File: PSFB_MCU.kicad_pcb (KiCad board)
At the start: 4 copper layers, 293 parts, among them J2 Power_IN, Q1 WMM043N10HGD, Q2 WMM043N10HGD, Q3 WMM043N10HGD, Q4 WMM043N10HGD, U10 USBLC6-2SC6, U11 USBLC6-2SC6, U12 USBLC6-2SC6, U13 USBLC6-2SC6, U14 USBLC6-2SC6, U17 TLV3501AIDBV, U19 TLV3501AIDBV, U20 TLV3501AIDBV, U4 AMS1117-5.0, U5 AMS1117-3.3, U6 LM5176PWP, U7 USBLC6-2SC6, U8 USBLC6-2SC6, U9 USBLC6-2SC6, Y1 16M

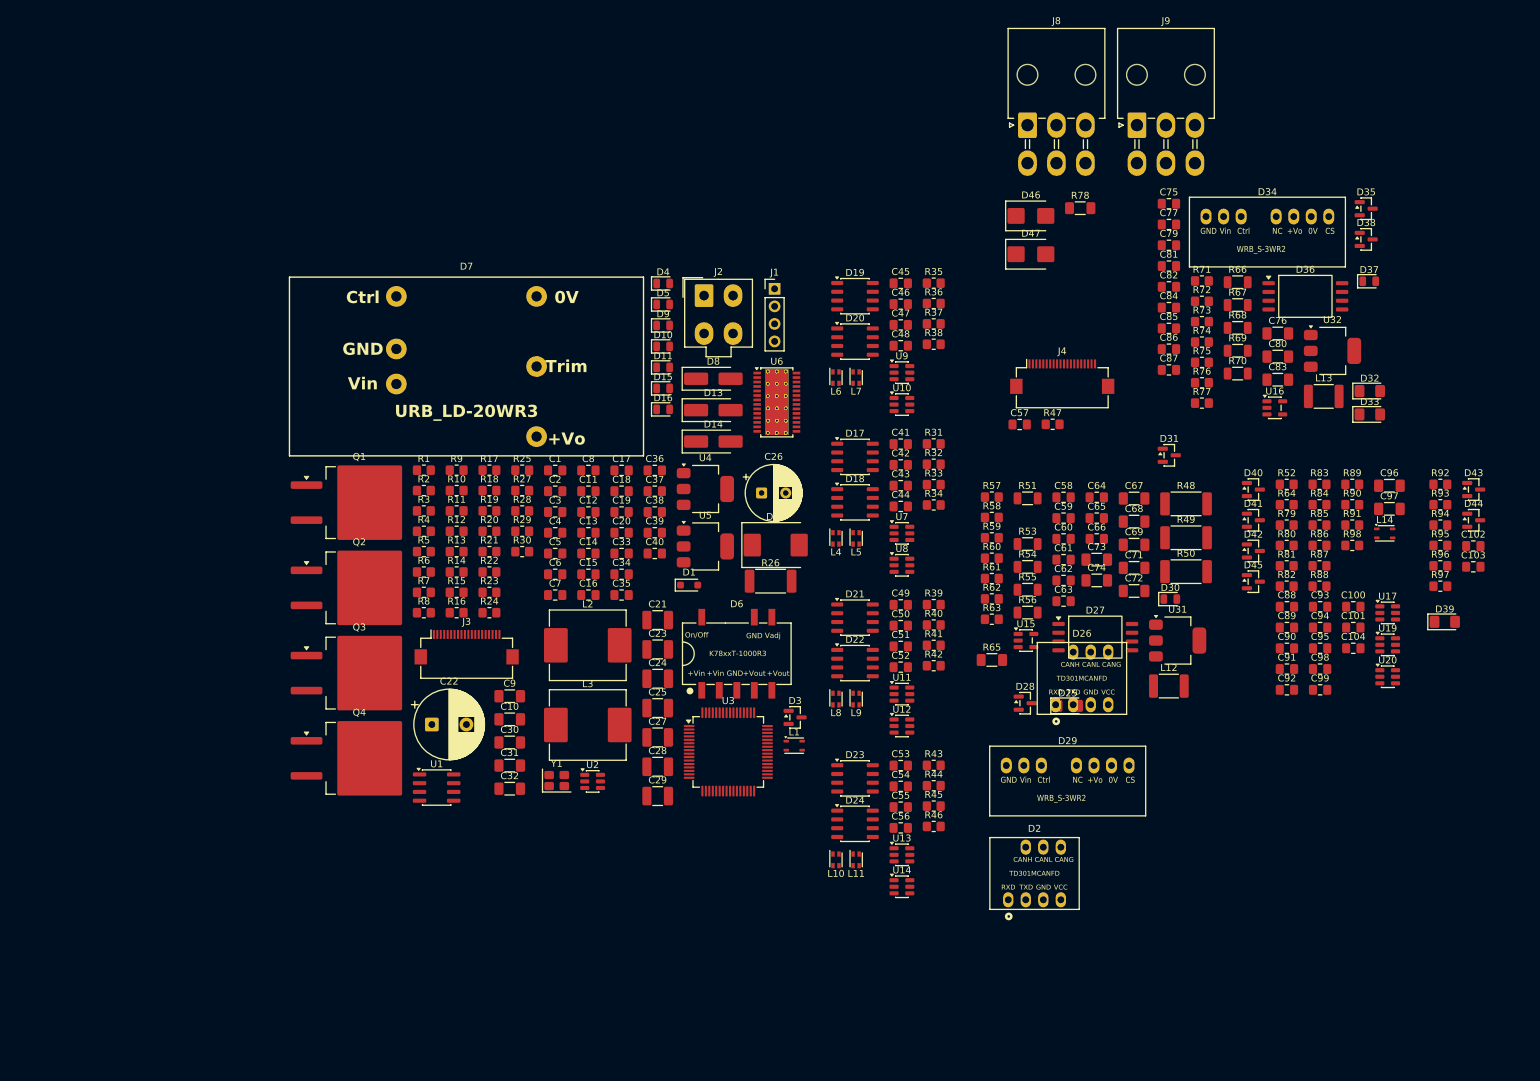
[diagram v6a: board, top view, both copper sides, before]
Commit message: VER1.0: добавил разделение питания VDD и VDDA
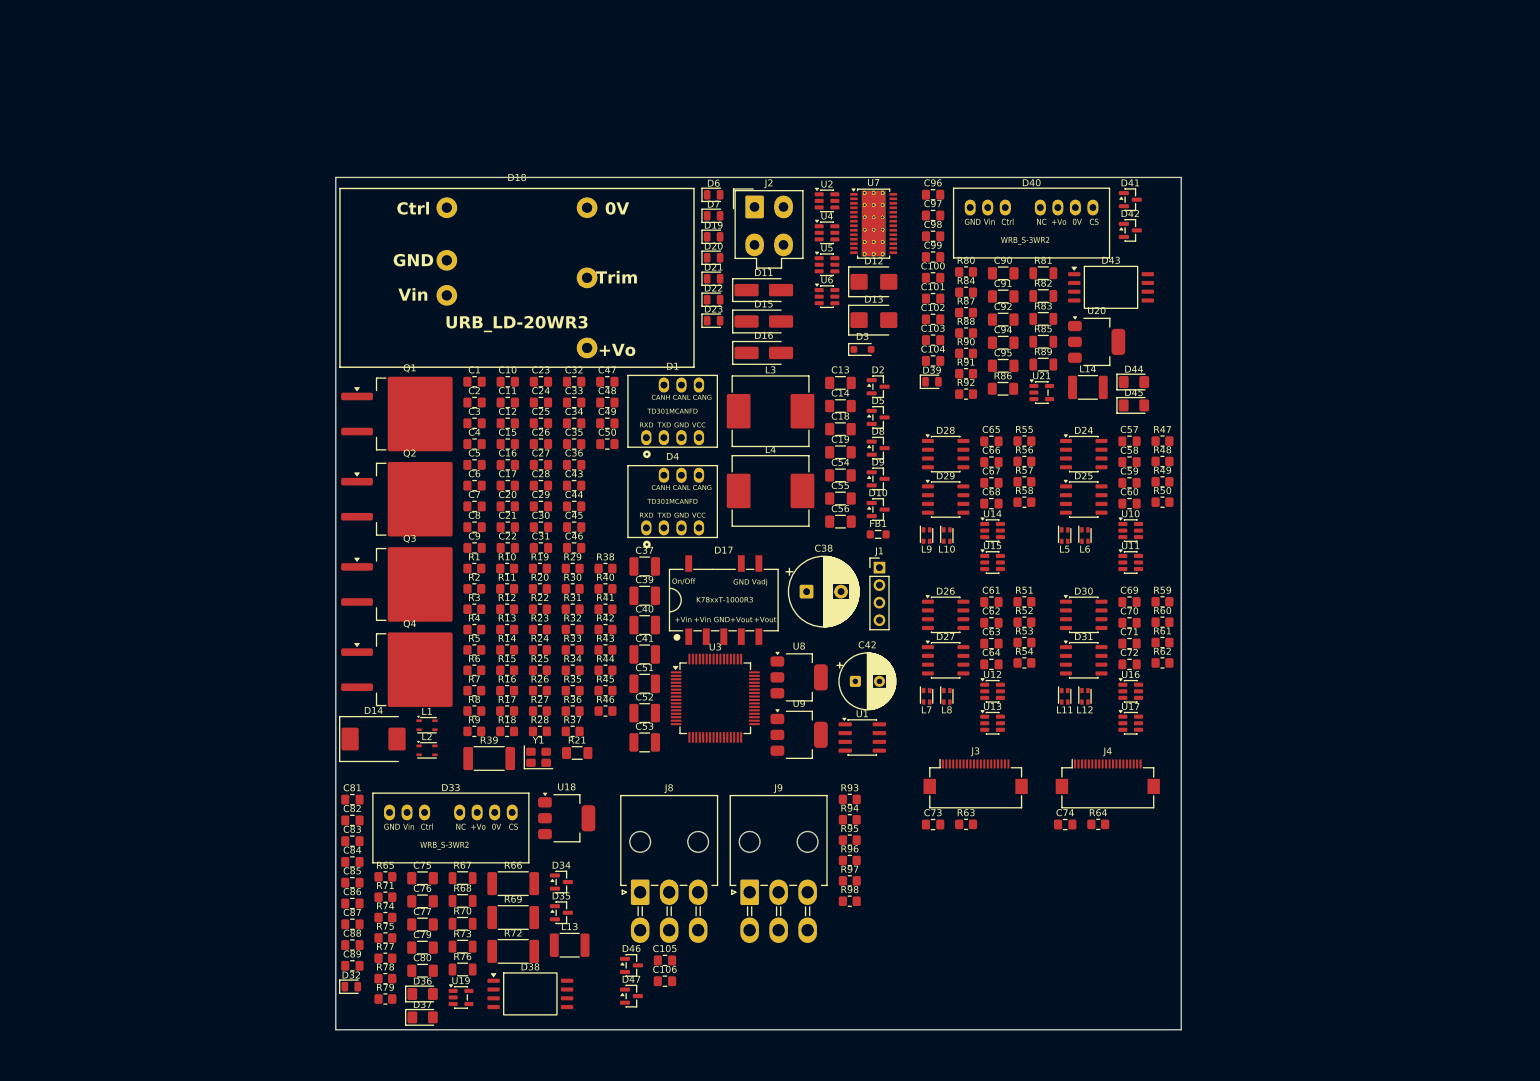
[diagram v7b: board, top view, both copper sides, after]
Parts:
- removed C93: 2.2u, Capacitor_SMD:C_0805_2012Metric_Pad1.18x1.45mm_HandSolder
- removed U31, U32: ~, Package_TO_SOT_SMD:SOT-223-3_TabPin2
- added C105: 330p, Capacitor_SMD:C_0805_2012Metric_Pad1.18x1.45mm_HandSolder, F.Cu at (130.2, 150.0)
- added C106: 330p, Capacitor_SMD:C_0805_2012Metric_Pad1.18x1.45mm_HandSolder, F.Cu at (130.2, 153.0)
- added C70: 4.7u, Capacitor_SMD:C_0805_2012Metric_Pad1.18x1.45mm_HandSolder, F.Cu at (197.5, 101.0)
- added FB1: ~, Inductor_SMD:L_0805_2012Metric_Pad1.05x1.20mm_HandSolder, F.Cu at (161.1, 88.2)
- added U18: ~, Package_TO_SOT_SMD:SOT-223-3_TabPin2, F.Cu at (116.0, 129.3)
- added U21: ~, Package_TO_SOT_SMD:SOT-23-5, F.Cu at (184.8, 67.7)
- C1: value 1u -> 100n
- C10: value 100n -> 10u; footprint Capacitor_SMD:C_1206_3216Metric_Pad1.33x1.80mm_HandSolder -> Capacitor_SMD:C_0805_2012Metric_Pad1.18x1.45mm_HandSolder
- C100: value 100n -> 56p
- C101, C86, C88: value 100n -> 2.2u
- C102: value 330p -> 0.1u
- C103: value 330p -> 2.2u
- C104: value 10n -> 0.1u
- C11: value 10n -> 1u
- C12, C59, C61: value 2.2u -> 100n
- C13, C77, C94: value 2.2u -> 10u; footprint Capacitor_SMD:C_0805_2012Metric_Pad1.18x1.45mm_HandSolder -> Capacitor_SMD:C_1206_3216Metric_Pad1.33x1.80mm_HandSolder
- C14: footprint Capacitor_SMD:C_0805_2012Metric_Pad1.18x1.45mm_HandSolder -> Capacitor_SMD:C_1206_3216Metric_Pad1.33x1.80mm_HandSolder
- C15, C20: value 100n -> 10n
- C16: value 4.7u -> 12p
- C17: value 1u -> 12p
- C18, C54, C92, C95: value 100n -> 10u; footprint Capacitor_SMD:C_0805_2012Metric_Pad1.18x1.45mm_HandSolder -> Capacitor_SMD:C_1206_3216Metric_Pad1.33x1.80mm_HandSolder
- C19: value 1u -> 100n; footprint Capacitor_SMD:C_0805_2012Metric_Pad1.18x1.45mm_HandSolder -> Capacitor_SMD:C_1206_3216Metric_Pad1.33x1.80mm_HandSolder
- C21: footprint Capacitor_SMD:C_1210_3225Metric_Pad1.33x2.70mm_HandSolder -> Capacitor_SMD:C_0805_2012Metric_Pad1.18x1.45mm_HandSolder
- C22: value 100u -> 2.2u; footprint Capacitor_THT:CP_Radial_D10.0mm_P5.00mm -> Capacitor_SMD:C_0805_2012Metric_Pad1.18x1.45mm_HandSolder
- C23: value 4.7u -> 2.2u; footprint Capacitor_SMD:C_1210_3225Metric_Pad1.33x2.70mm_HandSolder -> Capacitor_SMD:C_0805_2012Metric_Pad1.18x1.45mm_HandSolder
- C24, C28: value 10u -> 100n; footprint Capacitor_SMD:C_1210_3225Metric_Pad1.33x2.70mm_HandSolder -> Capacitor_SMD:C_0805_2012Metric_Pad1.18x1.45mm_HandSolder
- C25, C29: value 10u -> 10p; footprint Capacitor_SMD:C_1210_3225Metric_Pad1.33x2.70mm_HandSolder -> Capacitor_SMD:C_0805_2012Metric_Pad1.18x1.45mm_HandSolder
- C26: value 220u -> 100n; footprint Capacitor_THT:CP_Radial_D8.0mm_P3.50mm -> Capacitor_SMD:C_0805_2012Metric_Pad1.18x1.45mm_HandSolder
- C27: value 10u -> 2.2u; footprint Capacitor_SMD:C_1210_3225Metric_Pad1.33x2.70mm_HandSolder -> Capacitor_SMD:C_0805_2012Metric_Pad1.18x1.45mm_HandSolder
- C3, C4: value 12p -> 100n
- C30, C32, C67, C69, C71: value 10u -> 100n; footprint Capacitor_SMD:C_1206_3216Metric_Pad1.33x1.80mm_HandSolder -> Capacitor_SMD:C_0805_2012Metric_Pad1.18x1.45mm_HandSolder
- C31: value 10u -> 2.2u; footprint Capacitor_SMD:C_1206_3216Metric_Pad1.33x1.80mm_HandSolder -> Capacitor_SMD:C_0805_2012Metric_Pad1.18x1.45mm_HandSolder
- C33: value 33n -> 100n
- C34, C8: value 100n -> 1u
- C35: value 560p -> 100n
- C36: value 100n -> 10p
- C37: value 220p -> 2.2u; footprint Capacitor_SMD:C_0805_2012Metric_Pad1.18x1.45mm_HandSolder -> Capacitor_SMD:C_1210_3225Metric_Pad1.33x2.70mm_HandSolder
- C38: value 100n -> 100u; footprint Capacitor_SMD:C_0805_2012Metric_Pad1.18x1.45mm_HandSolder -> Capacitor_THT:CP_Radial_D10.0mm_P5.00mm
- C39: value 47p -> 4.7u; footprint Capacitor_SMD:C_0805_2012Metric_Pad1.18x1.45mm_HandSolder -> Capacitor_SMD:C_1210_3225Metric_Pad1.33x2.70mm_HandSolder
- C40: value 10n -> 10u; footprint Capacitor_SMD:C_0805_2012Metric_Pad1.18x1.45mm_HandSolder -> Capacitor_SMD:C_1210_3225Metric_Pad1.33x2.70mm_HandSolder
- C41, C53: value 100n -> 10u; footprint Capacitor_SMD:C_0805_2012Metric_Pad1.18x1.45mm_HandSolder -> Capacitor_SMD:C_1210_3225Metric_Pad1.33x2.70mm_HandSolder
- C42: value 4.7u -> 220u; footprint Capacitor_SMD:C_0805_2012Metric_Pad1.18x1.45mm_HandSolder -> Capacitor_THT:CP_Radial_D8.0mm_P3.50mm
- C44: value 4.7u -> 33n
- C46: value 100n -> 560p
- C47: value 4.7u -> 100n
- C48: value 4.7u -> 220p
- C50: value 100n -> 47p
- C51, C52: value 4.7u -> 10u; footprint Capacitor_SMD:C_0805_2012Metric_Pad1.18x1.45mm_HandSolder -> Capacitor_SMD:C_1210_3225Metric_Pad1.33x2.70mm_HandSolder
- C55, C56: value 4.7u -> 10u; footprint Capacitor_SMD:C_0805_2012Metric_Pad1.18x1.45mm_HandSolder -> Capacitor_SMD:C_1206_3216Metric_Pad1.33x1.80mm_HandSolder
- C57: value 10n -> 100n
- C58, C64: value 56p -> 4.7u
- C60, C62: value 0.1u -> 4.7u
- C63: value 56p -> 100n
- C66: value 1n -> 4.7u
- C68: value 1u -> 4.7u; footprint Capacitor_SMD:C_1206_3216Metric_Pad1.33x1.80mm_HandSolder -> Capacitor_SMD:C_0805_2012Metric_Pad1.18x1.45mm_HandSolder
- C7: value 100n -> 4.7u
- C72: value 10u -> 4.7u; footprint Capacitor_SMD:C_1206_3216Metric_Pad1.33x1.80mm_HandSolder -> Capacitor_SMD:C_0805_2012Metric_Pad1.18x1.45mm_HandSolder
- C73: value 10u -> 10n; footprint Capacitor_SMD:C_1206_3216Metric_Pad1.33x1.80mm_HandSolder -> Capacitor_SMD:C_0805_2012Metric_Pad1.18x1.45mm_HandSolder
- C74: value 1u -> 10n; footprint Capacitor_SMD:C_1206_3216Metric_Pad1.33x1.80mm_HandSolder -> Capacitor_SMD:C_0805_2012Metric_Pad1.18x1.45mm_HandSolder
- C75: value 56p -> 10u; footprint Capacitor_SMD:C_0805_2012Metric_Pad1.18x1.45mm_HandSolder -> Capacitor_SMD:C_1206_3216Metric_Pad1.33x1.80mm_HandSolder
- C76: value 10u -> 1u
- C79: value 0.1u -> 10u; footprint Capacitor_SMD:C_0805_2012Metric_Pad1.18x1.45mm_HandSolder -> Capacitor_SMD:C_1206_3216Metric_Pad1.33x1.80mm_HandSolder
- C81: value 2.2u -> 56p
- C82: value 0.1u -> 100n
- C83, C96: value 10u -> 56p; footprint Capacitor_SMD:C_1206_3216Metric_Pad1.33x1.80mm_HandSolder -> Capacitor_SMD:C_0805_2012Metric_Pad1.18x1.45mm_HandSolder
- C84: value 56p -> 1n
- C87: value 1n -> 0.1u
- C89: value 10p -> 0.1u
- C9, C97: footprint Capacitor_SMD:C_1206_3216Metric_Pad1.33x1.80mm_HandSolder -> Capacitor_SMD:C_0805_2012Metric_Pad1.18x1.45mm_HandSolder
- C90: value 10p -> 10u; footprint Capacitor_SMD:C_0805_2012Metric_Pad1.18x1.45mm_HandSolder -> Capacitor_SMD:C_1206_3216Metric_Pad1.33x1.80mm_HandSolder
- C91: value 100n -> 1u; footprint Capacitor_SMD:C_0805_2012Metric_Pad1.18x1.45mm_HandSolder -> Capacitor_SMD:C_1206_3216Metric_Pad1.33x1.80mm_HandSolder
- C98: value 10p -> 56p
- C99: value 2.2u -> 1n
- D1: footprint Diode_SMD:D_SOD-323_HandSoldering -> MORNSUN:TD5(3)01MCANFD
- D10, D5, D9: footprint LED_SMD:LED_0805_2012Metric -> Package_TO_SOT_SMD:SOT-23
- D11, D15, D16: footprint LED_SMD:LED_0805_2012Metric -> Diode_SMD:D_SMA_Handsoldering
- D12: value D_TVS_Small -> ~; footprint Diode_SMD:D_SMC -> Diode_SMD:D_SMB
- D13: value D_Schottky_Small -> ~; footprint Diode_SMD:D_SMA_Handsoldering -> Diode_SMD:D_SMB
- D14: value D_Schottky_Small -> ~; footprint Diode_SMD:D_SMA_Handsoldering -> Diode_SMD:D_SMC
- D17: footprint Package_SO:SO-8_3.9x4.9mm_P1.27mm -> MORNSUN:K78xxT-1000R3
- D18: footprint Package_SO:SO-8_3.9x4.9mm_P1.27mm -> MORNSUN:URB_LD-20WR3
- D19, D20, D21, D22, D23: footprint Package_SO:SO-8_3.9x4.9mm_P1.27mm -> LED_SMD:LED_0805_2012Metric
- D2: value TD301MCANFD -> ~; footprint MORNSUN:TD5(3)01MCANFD -> Package_TO_SOT_SMD:SOT-23
- D25: footprint LED_SMD:LED_1206_3216Metric_Pad1.42x1.75mm_HandSolder -> Package_SO:SO-8_3.9x4.9mm_P1.27mm
- D26: value TD301MCANFD -> ~; footprint MORNSUN:TD5(3)01MCANFD -> Package_SO:SO-8_3.9x4.9mm_P1.27mm
- D27: footprint Package_SO:SOIC-8_7.5x5.85mm_P1.27mm -> Package_SO:SO-8_3.9x4.9mm_P1.27mm
- D28, D31: footprint Package_TO_SOT_SMD:SOT-23 -> Package_SO:SO-8_3.9x4.9mm_P1.27mm
- D29: footprint MORNSUN:WRB_S-3WR2 -> Package_SO:SO-8_3.9x4.9mm_P1.27mm
- D3: footprint Package_TO_SOT_SMD:SOT-23 -> Diode_SMD:D_SOD-323_HandSoldering
- D30: footprint LED_SMD:LED_0805_2012Metric -> Package_SO:SO-8_3.9x4.9mm_P1.27mm
- D32, D39: footprint LED_SMD:LED_1206_3216Metric_Pad1.42x1.75mm_HandSolder -> LED_SMD:LED_0805_2012Metric
- D33: footprint LED_SMD:LED_1206_3216Metric_Pad1.42x1.75mm_HandSolder -> MORNSUN:WRB_S-3WR2
- D34: footprint MORNSUN:WRB_S-3WR2 -> Package_TO_SOT_SMD:SOT-23
- D36: footprint Package_SO:SOIC-8_7.5x5.85mm_P1.27mm -> LED_SMD:LED_1206_3216Metric_Pad1.42x1.75mm_HandSolder
- D37: footprint LED_SMD:LED_0805_2012Metric -> LED_SMD:LED_1206_3216Metric_Pad1.42x1.75mm_HandSolder
- D38, D43: footprint Package_TO_SOT_SMD:SOT-23 -> Package_SO:SOIC-8_7.5x5.85mm_P1.27mm
- D4: footprint LED_SMD:LED_0805_2012Metric -> MORNSUN:TD5(3)01MCANFD
- D40: footprint Package_TO_SOT_SMD:SOT-23 -> MORNSUN:WRB_S-3WR2
- D44, D45: footprint Package_TO_SOT_SMD:SOT-23 -> LED_SMD:LED_1206_3216Metric_Pad1.42x1.75mm_HandSolder
- D46: value D_TVS_Small -> ~; footprint Diode_SMD:D_SMB -> Package_TO_SOT_SMD:SOT-23
- D47: value D_Small -> ~; footprint Diode_SMD:D_SMB -> Package_TO_SOT_SMD:SOT-23
- D6: value K7809T -> ~; footprint MORNSUN:K78xxT-1000R3 -> LED_SMD:LED_0805_2012Metric
- D7: value URB2415LD-20WR3 -> ~; footprint MORNSUN:URB_LD-20WR3 -> LED_SMD:LED_0805_2012Metric
- D8: value D_Schottky_Small -> ~; footprint Diode_SMD:D_SMA_Handsoldering -> Package_TO_SOT_SMD:SOT-23
- J2: value Power_IN -> ~
- L10, L11, L5, L6, L7, L8, L9: value DLW21SN900SQ2L -> ~
- L12: value 4.7u -> ~; footprint Inductor_SMD:L_1812_4532Metric_Pad1.30x3.40mm_HandSolder -> Inductor_SMD:L_CommonModeChoke_Coilcraft_0805USB
- L14: value ~ -> 4.7u; footprint Inductor_SMD:L_CommonModeChoke_TDK_ACM2520-2P -> Inductor_SMD:L_1812_4532Metric_Pad1.30x3.40mm_HandSolder
- L2: value 10u -> ~; footprint Inductor_SMD:L_Panasonic_PCC-M1040ML -> Inductor_SMD:L_CommonModeChoke_TDK_ACM2520-2P
- L4: value DLW21SN900SQ2L -> 10u; footprint Inductor_SMD:L_CommonModeChoke_Coilcraft_0805USB -> Inductor_SMD:L_Panasonic_PCC-M1040ML
- Q1, Q2, Q3, Q4: value WMM043N10HGD -> ~
- R1, R2: value 10k -> 59
- R10: value 10 -> 1k
- R11: value 1k -> 100
- R13, R29: value 3k -> 1k
- R15: value 249k -> 100
- R16: value 59k -> 0
- R17: value 10k -> 1k
- R18: value 240k -> 0
- R19: value 93.1k -> 1k
- R20: value 51k -> 100
- R21: value 143k -> 10; footprint Resistor_SMD:R_0805_2012Metric_Pad1.20x1.40mm_HandSolder -> Resistor_SMD:R_1206_3216Metric_Pad1.30x1.75mm_HandSolder
- R22: value 10k -> 0
- R23: value 10k -> 2k
- R24: value 100 -> 10
- R25, R41, R44, R79, R88: value 0 -> 1k
- R26: value 10m -> 249k; footprint Resistor_SMD:R_2512_6332Metric_Pad1.40x3.35mm_HandSolder -> Resistor_SMD:R_0805_2012Metric_Pad1.20x1.40mm_HandSolder
- R27: value 100 -> 59k
- R28, R47: value 470 -> 0
- R3, R4: value 20 -> 10k
- R30: value 3k -> 10k
- R31: value 0 -> 240k
- R32: value 0 -> 93.1k
- R33: value 0 -> 51k
- R34: value 0 -> 143k
- R35, R36: value 0 -> 10k
- R37, R40: value 0 -> 100
- R39: value 0 -> 10m; footprint Resistor_SMD:R_0805_2012Metric_Pad1.20x1.40mm_HandSolder -> Resistor_SMD:R_2512_6332Metric_Pad1.40x3.35mm_HandSolder
- R43, R45, R46: value 0 -> 3k
- R48, R49, R50: value 150k -> 0; footprint Resistor_SMD:R_2512_6332Metric_Pad1.40x3.35mm_HandSolder -> Resistor_SMD:R_0805_2012Metric_Pad1.20x1.40mm_HandSolder
- R5, R6: value 59 -> 20
- R51, R53, R54, R55: value 2M -> 0; footprint Resistor_SMD:R_1206_3216Metric -> Resistor_SMD:R_0805_2012Metric_Pad1.20x1.40mm_HandSolder
- R52, R58, R59, R60, R61: value 1k -> 0
- R56: value 11.3k -> 0; footprint Resistor_SMD:R_1206_3216Metric -> Resistor_SMD:R_0805_2012Metric_Pad1.20x1.40mm_HandSolder
- R57: value 120 -> 0
- R62: value 510 -> 0
- R63: value 750 -> 470
- R64: value 1k -> 470
- R65: value 10k -> 750; footprint Resistor_SMD:R_1206_3216Metric_Pad1.30x1.75mm_HandSolder -> Resistor_SMD:R_0805_2012Metric_Pad1.20x1.40mm_HandSolder
- R66, R69: value 110k -> 150k; footprint Resistor_SMD:R_1206_3216Metric -> Resistor_SMD:R_2512_6332Metric_Pad1.40x3.35mm_HandSolder
- R67, R68: value 110k -> 2M
- R7, R8: value 1k -> 59
- R70: value 11.3k -> 2M
- R71: value 120 -> 1k
- R72: value 1k -> 150k; footprint Resistor_SMD:R_0805_2012Metric_Pad1.20x1.40mm_HandSolder -> Resistor_SMD:R_2512_6332Metric_Pad1.40x3.35mm_HandSolder
- R73: value 1k -> 2M; footprint Resistor_SMD:R_0805_2012Metric_Pad1.20x1.40mm_HandSolder -> Resistor_SMD:R_1206_3216Metric
- R74: value 750 -> 120
- R76: value 1k -> 11.3k; footprint Resistor_SMD:R_0805_2012Metric_Pad1.20x1.40mm_HandSolder -> Resistor_SMD:R_1206_3216Metric
- R78: value 10 -> 1k; footprint Resistor_SMD:R_1206_3216Metric_Pad1.30x1.75mm_HandSolder -> Resistor_SMD:R_0805_2012Metric_Pad1.20x1.40mm_HandSolder
- R80: value 100 -> 750
- R81: value 100 -> 110k; footprint Resistor_SMD:R_0805_2012Metric_Pad1.20x1.40mm_HandSolder -> Resistor_SMD:R_1206_3216Metric
- R82, R83: value 0 -> 110k; footprint Resistor_SMD:R_0805_2012Metric_Pad1.20x1.40mm_HandSolder -> Resistor_SMD:R_1206_3216Metric
- R85: value 1k -> 110k; footprint Resistor_SMD:R_0805_2012Metric_Pad1.20x1.40mm_HandSolder -> Resistor_SMD:R_1206_3216Metric
- R86: value 59 -> 10k; footprint Resistor_SMD:R_0805_2012Metric_Pad1.20x1.40mm_HandSolder -> Resistor_SMD:R_1206_3216Metric_Pad1.30x1.75mm_HandSolder
- R87: value 100 -> 120
- R89: value 0 -> 11.3k; footprint Resistor_SMD:R_0805_2012Metric_Pad1.20x1.40mm_HandSolder -> Resistor_SMD:R_1206_3216Metric
- R9, R92: value 2k -> 1k
- R90: value 1k -> 510
- R93: value 3k -> 2k
- R95: value 120 -> 3k
- R97: value 3k -> 120
- R98: value 59 -> 3k
- U10, U11, U12, U13, U14: value USBLC6-2SC6 -> ~
- U15, U16: footprint Package_TO_SOT_SMD:SOT-23-5 -> Package_TO_SOT_SMD:SOT-23-6
- U17: value TLV3501AIDBV -> ~
- U19: value TLV3501AIDBV -> ~; footprint Package_TO_SOT_SMD:SOT-23-6 -> Package_TO_SOT_SMD:SOT-23-5
- U20: value TLV3501AIDBV -> ~; footprint Package_TO_SOT_SMD:SOT-23-6 -> Package_TO_SOT_SMD:SOT-223-3_TabPin2
- U4: value AMS1117-5.0 -> ~; footprint Package_TO_SOT_SMD:SOT-223-3_TabPin2 -> Package_TO_SOT_SMD:SOT-23-6
- U5: value AMS1117-3.3 -> ~; footprint Package_TO_SOT_SMD:SOT-223-3_TabPin2 -> Package_TO_SOT_SMD:SOT-23-6
- U6: value LM5176PWP -> ~; footprint Package_SO:HTSSOP-28-1EP_4.4x9.7mm_P0.65mm_EP3.4x9.5mm_ThermalVias -> Package_TO_SOT_SMD:SOT-23-6
- U7: value USBLC6-2SC6 -> ~; footprint Package_TO_SOT_SMD:SOT-23-6 -> Package_SO:HTSSOP-28-1EP_4.4x9.7mm_P0.65mm_EP3.4x9.5mm_ThermalVias
- U8, U9: value USBLC6-2SC6 -> ~; footprint Package_TO_SOT_SMD:SOT-23-6 -> Package_TO_SOT_SMD:SOT-223-3_TabPin2
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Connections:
- C100 pad 1: +3.3V -> Net-(U21--)
- C100 pad 2: GND -> Net-(C100-Pad2)
- C101 pad 1: Net-(U20--) -> GND_OUT
- C101 pad 2: GND -> +3.3VP
- C102 pad 1: /Current_measure_1 -> +3.3VP
- C102 pad 2: GND -> GND_OUT
- C103 pad 1: /Current_measure_2 -> GND
- C103 pad 2: GND -> +3.3VA
- C104 pad 1: Net-(C104-Pad1) -> +3.3VA
- C104 pad 2: GND_CAN2 -> GND
- C11 pad 1: Net-(C11-Pad1) -> +3.3V
- C11 pad 2: GND_CAN1 -> GND
- C12 pad 1: Net-(U3-VCAP_1) -> GND
- C12 pad 2: GND -> NRST
- C13 pad 1: Net-(U3-VCAP_2) -> +3.3V
- C15 pad 1: +3.3V -> Net-(C15-Pad1)
- C15 pad 2: GND -> GND_CAN1
- C16 pad 1: +3.3V -> GND
- C16 pad 2: GND -> Net-(U3-PH0)
- C17 pad 1: +3.3V -> Net-(U3-PH1)
- C18 pad 1: Net-(U6-VIN) -> +3.3V
- C18 pad 2: GND_IN -> GND
- C19 pad 1: VCC -> +3.3V
- C19 pad 2: GND_IN -> GND
- C2 pad 1: GND -> +3.3V
- C2 pad 2: NRST -> GND
- C20 pad 1: +24V -> Net-(C20-Pad1)
- C20 pad 2: GND_IN -> GND_CAN2
- C21 pad 1: GND_IN -> Net-(U3-VCAP_1)
- C21 pad 2: Net-(D12-A2) -> GND
- C22 pad 1: Net-(D12-A2) -> Net-(U3-VCAP_2)
- C22 pad 2: GND_IN -> GND
- C23 pad 1: GND_IN -> +3.3VA
- C23 pad 2: Net-(D12-A2) -> GND
- C24 pad 1: GND_IN -> +3.3VA
- C24 pad 2: +24V -> GND
- C25 pad 1: GND_IN -> /OverVoltage
- C25 pad 2: +24V -> GND
- C26 pad 1: +24V -> Net-(U4--)
- C26 pad 2: GND_IN -> GND
- C27 pad 1: GND_IN -> +3.3VA
- C27 pad 2: +24V -> GND
- C28 pad 1: GND -> +3.3VA
- C28 pad 2: +15V -> GND
- C29 pad 1: GND -> /BkIN_1
- C29 pad 2: +9V -> GND
- C3 pad 1: GND -> +3.3V
- C3 pad 2: Net-(U3-PH0) -> GND
- C30 pad 1: GND -> Net-(U5--)
- C30 pad 2: +5V -> GND
- C31 pad 1: GND -> +3.3VA
- C31 pad 2: +5V -> GND
- C32 pad 1: GND -> +3.3VA
- C32 pad 2: +3.3V -> GND
- C33 pad 1: Net-(U6-COMP) -> Net-(U7-VIN)
- C33 pad 2: Net-(C33-Pad2) -> GND_IN
- C34 pad 1: Net-(U6-SS) -> VCC
- C35 pad 1: Net-(U6-COMP) -> +24V
- C36 pad 1: /SW1 -> /BkIN_8
- C36 pad 2: Net-(D13-K) -> GND
- C37 pad 1: Net-(U6-SLOPE) -> GND_IN
- C37 pad 2: GND_IN -> Net-(D14-A2)
- C38 pad 1: /SW2 -> Net-(D14-A2)
- C38 pad 2: Net-(D14-K) -> GND_IN
- C39 pad 1: Net-(U6-CSG) -> GND_IN
- C39 pad 2: Net-(U6-CS) -> Net-(D14-A2)
- C4 pad 1: Net-(U3-PH1) -> +3.3V
- C40 pad 1: /ERROR_Channel_1 -> GND_IN
- C40 pad 2: GND -> +24V
- C41 pad 1: +3.3V -> GND_IN
- C41 pad 2: GND -> +24V
- C42 pad 1: +3.3V -> +24V
- C42 pad 2: GND -> GND_IN
- C43 pad 1: +3.3V -> Net-(U6--)
- C44 pad 1: +3.3V -> Net-(U7-COMP)
- C44 pad 2: GND -> Net-(C44-Pad2)
- C45 pad 1: +3.3V -> Net-(U7-SS)
- C45 pad 2: GND -> GND_IN
- C46 pad 1: +3.3V -> Net-(U7-COMP)
- C46 pad 2: GND -> GND_IN
- C47 pad 1: +3.3V -> /SW1
- C47 pad 2: GND -> Net-(D15-K)
- C48 pad 1: +3.3V -> Net-(U7-SLOPE)
- C48 pad 2: GND -> GND_IN
- C49 pad 1: +3.3V -> /SW2
- C49 pad 2: GND -> Net-(D16-K)
- C50 pad 1: +3.3V -> Net-(U7-CSG)
- C50 pad 2: GND -> Net-(U7-CS)
- C51 pad 1: +3.3V -> GND_IN
- C51 pad 2: GND -> +24V
- C52 pad 1: +3.3V -> GND
- C52 pad 2: GND -> +15V
- C53 pad 1: +3.3V -> GND
- C53 pad 2: GND -> +9V
- C54 pad 1: +3.3V -> GND
- C54 pad 2: GND -> +5V
- C55 pad 1: +3.3V -> GND
- C55 pad 2: GND -> +5V
- C56 pad 1: +3.3V -> GND
- C56 pad 2: GND -> +3.3V
- C57 pad 1: /ERROR_Channel_2 -> +3.3V
- C58 pad 1: Net-(D27-VIN) -> +3.3V
- C58 pad 2: GNDPWR -> GND
- C59 pad 1: GNDPWR -> +3.3V
- C59 pad 2: +3.3VP -> GND
- C60 pad 1: +3.3VP -> +3.3V
- C60 pad 2: GNDPWR -> GND
- C61 pad 1: GND -> +3.3V
- C61 pad 2: +3.3V -> GND
- C63 pad 1: GND -> +3.3V
- C63 pad 2: Net-(U15-+) -> GND
- C64 pad 1: Net-(U15--) -> +3.3V
- C64 pad 2: Net-(C64-Pad2) -> GND
- C66 pad 1: /HVDC_MCU -> +3.3V
- C67 pad 1: +24V -> +3.3V
- C67 pad 2: GND_IN -> GND
- C68 pad 1: Net-(D29-Vin) -> +3.3V
- C68 pad 2: GND_IN -> GND
- C69 pad 1: GNDPWR -> +3.3V
- C69 pad 2: Net-(D29-CS) -> GND
- C71 pad 1: GNDPWR -> +3.3V
- C71 pad 2: Net-(D29-+Vo) -> GND
- C72 pad 1: GNDPWR -> +3.3V
- C72 pad 2: +3.3VP -> GND
- C73 pad 1: +24V -> /ERROR_Channel_1
- C73 pad 2: GND_IN -> GND
- C74 pad 1: Net-(D34-Vin) -> /ERROR_Channel_2
- C74 pad 2: GND_IN -> GND
- C75 pad 1: Net-(D35-common) -> +24V
- C75 pad 2: GND_OUT -> GND_IN
- C76 pad 1: GND_OUT -> Net-(D33-Vin)
- C76 pad 2: Net-(D34-CS) -> GND_IN
- C77 pad 1: GND_OUT -> GNDPWR
- C77 pad 2: +3.3VP -> Net-(D33-CS)
- C79 pad 1: +3.3VP -> GNDPWR
- C79 pad 2: GND_OUT -> Net-(D33-+Vo)
- C80 pad 1: GND_OUT -> GNDPWR
- C80 pad 2: Net-(D34-+Vo) -> +3.3VP
- C81 pad 2: +3.3V -> Net-(U19-+)
- C82 pad 1: +3.3V -> +3.3VA
- C83 pad 1: GND_OUT -> Net-(D34-common)
- C83 pad 2: +3.3VP -> GNDPWR
- C84 pad 1: GND -> /HVDC_MCU
- C84 pad 2: Net-(U16-+) -> GND
- C85 pad 1: Net-(U16--) -> Net-(U19--)
- C86 pad 1: +3.3V -> GNDPWR
- C86 pad 2: GND -> +3.3VP
- C87 pad 1: /LVDC_MCU -> +3.3VP
- C87 pad 2: GND -> GNDPWR
- C88 pad 1: Net-(U17--) -> GND
- C88 pad 2: GND -> +3.3VA
- C89 pad 1: /OverVoltage -> +3.3VA
- C9 pad 1: +3.3V -> +3.3VA
- C90 pad 1: /BkIN_1 -> +24V
- C90 pad 2: GND -> GND_IN
- C91 pad 1: Net-(U19--) -> Net-(D40-Vin)
- C91 pad 2: GND -> GND_IN
- C92 pad 1: +3.3V -> GND_OUT
- C92 pad 2: GND -> Net-(D40-CS)
- C94 pad 1: +3.3V -> GND_OUT
- C94 pad 2: GND -> Net-(D40-+Vo)
- C95 pad 1: +3.3V -> GND_OUT
- C95 pad 2: GND -> +3.3VP
- C96 pad 1: +3.3V -> GND
- C96 pad 2: GND -> Net-(U21-+)
- C97 pad 1: +3.3V -> +3.3VA
- C98 pad 1: /BkIN_8 -> Net-(D41-common)
- C98 pad 2: GND -> GND_OUT
- C99 pad 1: +3.3V -> /LVDC_MCU
- D1 pad 1: +3.3V -> /CAN1_RXD_MCU
- D1 pad 2: Net-(D1-A) -> /CAN1_TXD_MCU
- D10 pad 1: Net-(D10-K) -> GND
- D10 pad 2: +15V -> +3.3VA
- D11 pad 2: +3.3V -> VIN_filtered
- D12 pad 1: GND_IN -> Net-(D12-K)
- D12 pad 2: Net-(D12-A2) -> VIN
- D13 pad 1: Net-(D13-K) -> GND_IN
- D13 pad 2: VCC -> VIN_filtered
- D14 pad 1: Net-(D14-K) -> GND_IN
- D14 pad 2: VCC -> Net-(D14-A2)
- D15 pad 2: VIN -> VCC
- D16 pad 2: +24V -> VCC
- D17 pad 1: unconnected-(D17-RO-Pad1) -> +15V
- D17 pad 2: GND -> +15V
- D17 pad 3: +3.3V -> GND
- D17 pad 4: /TMR1_CH1N -> +9V
- D17 pad 5: GND -> +9V
- D17 pad 6: Net-(D17-A) -> unconnected-(D17-Vadj-Pad6)
- D17 pad 7: Net-(D17-B) -> GND
- D18 pad 2: GND -> GND_IN
- D18 pad 3: +3.3V -> +24V
- D18 pad 4: /TMR1_CH1 -> +15V
- D18 pad 5: GND -> Net-(D18-Trim)
- D18 pad 6: Net-(D18-A) -> GND1
- D19 pad 1: unconnected-(D19-RO-Pad1) -> Net-(D19-K)
- D19 pad 2: GND -> +5V
- D2 pad 1: /CAN1_RXD_MCU -> /CANH_1
- D2 pad 2: /CAN1_TXD_MCU -> /CANL_1
- D2 pad 3: GND -> GND_CAN1
- D20 pad 1: unconnected-(D20-RO-Pad1) -> Net-(D20-K)
- D20 pad 2: GND -> +15V
- D21 pad 1: unconnected-(D21-RO-Pad1) -> Net-(D21-K)
- D21 pad 2: GND -> +3.3V
- D22 pad 1: unconnected-(D22-RO-Pad1) -> Net-(D22-K)
- D22 pad 2: GND -> VIN
- D23 pad 1: unconnected-(D23-RO-Pad1) -> Net-(D23-K)
- D23 pad 2: GND -> +24V
- D24 pad 4: /TMR8_CH2 -> /TMR1_CH1N
- D25 pad 1: GNDPWR -> unconnected-(D25-RO-Pad1)
- D25 pad 2: Net-(D25-A) -> GND
- D26 pad 1: /CAN2_RXD_MCU -> unconnected-(D26-RO-Pad1)
- D26 pad 2: /CAN2_TXD_MCU -> GND
- D26 pad 3: GND -> +3.3V
- D26 pad 4: +3.3V -> /TMR1_CH2N
- D26 pad 5: GND_CAN2 -> GND
- D26 pad 6: Net-(D26-CANL) -> Net-(D26-A)
- D26 pad 7: Net-(D26-CANH) -> Net-(D26-B)
- D27 pad 1: +3.3VP -> unconnected-(D27-RO-Pad1)
- D27 pad 2: Net-(D27-VIN) -> GND
- D27 pad 3: GNDPWR -> +3.3V
- D27 pad 4: GNDPWR -> /TMR1_CH2
- D27 pad 6: Net-(D27-OUTN) -> Net-(D27-A)
- D27 pad 7: Net-(D27-OUTP) -> Net-(D27-B)
- D28 pad 1: GND -> unconnected-(D28-RO-Pad1)
- D28 pad 2: +3.3V -> GND
- D28 pad 3: /HVDC_MCU -> +3.3V
- D29 pad 1: GND_IN -> unconnected-(D29-RO-Pad1)
- D29 pad 2: Net-(D29-Vin) -> GND
- D29 pad 3: unconnected-(D29-Ctrl-Pad3) -> +3.3V
- D29 pad 5: unconnected-(D29-NC-Pad5) -> GND
- D29 pad 6: Net-(D29-+Vo) -> Net-(D29-A)
- D29 pad 7: GNDPWR -> Net-(D29-B)
- D29 pad 8: Net-(D29-CS) -> +3.3V
- D3 pad 1: /CANH_1 -> +3.3V
- D3 pad 2: /CANL_1 -> Net-(D3-A)
- D30 pad 1: Net-(D30-K) -> unconnected-(D30-RO-Pad1)
- D30 pad 2: +3.3VP -> GND
- D31 pad 1: GNDPWR -> unconnected-(D31-RO-Pad1)
- D31 pad 2: +3.3VP -> GND
- D31 pad 3: Net-(D27-VIN) -> +3.3V
- D32 pad 1: GND_OUT -> Net-(D32-K)
- D32 pad 2: Net-(D32-A) -> +3.3VP
- D33 pad 1: Net-(D32-A) -> GND_IN
- D33 pad 2: GND_OUT -> Net-(D33-Vin)
- D34 pad 1: GND_IN -> GNDPWR
- D34 pad 2: Net-(D34-Vin) -> +3.3VP
- D34 pad 3: unconnected-(D34-Ctrl-Pad3) -> Net-(D34-common)
- D35 pad 1: GND_OUT -> GND
- D35 pad 2: +3.3VP -> +3.3VA
- D35 pad 3: Net-(D35-common) -> /HVDC_MCU
- D36 pad 1: +3.3VP -> Net-(D36-K)
- D36 pad 2: Net-(D35-common) -> GNDPWR
- D37 pad 1: Net-(D37-K) -> GNDPWR
- D37 pad 2: +3.3VP -> Net-(D36-K)
- D38 pad 1: GND -> +3.3VP
- D38 pad 2: +3.3V -> Net-(D34-common)
- D38 pad 3: /LVDC_MCU -> GNDPWR
- D39 pad 1: Net-(D25-A) -> Net-(D39-K)
- D39 pad 2: GNDPWR -> +3.3VP
- D4 pad 1: Net-(D4-K) -> /CAN2_RXD_MCU
- D4 pad 2: Net-(D4-A) -> /CAN2_TXD_MCU
- D40 pad 1: GND -> GND_IN
- D40 pad 2: +3.3V -> Net-(D40-Vin)
- D40 pad 3: /OverVoltage -> unconnected-(D40-Ctrl-Pad3)
- D41 pad 1: GND -> GND_OUT
- D41 pad 2: +3.3V -> +3.3VP
- D41 pad 3: /BkIN_1 -> Net-(D41-common)
- D42 pad 2: +3.3V -> +3.3VA
- D42 pad 3: /BkIN_8 -> /LVDC_MCU
- D43 pad 1: GND -> +3.3VP
- D43 pad 2: +3.3V -> Net-(D41-common)
- D43 pad 3: /Current_measure_1 -> GND_OUT
- D44 pad 1: GND -> Net-(D44-K)
- D44 pad 2: +3.3V -> GND_OUT
- D45 pad 1: /CANH_2 -> GND_OUT
- D45 pad 2: /CANL_2 -> Net-(D44-K)
- D46 pad 1: GND_IN -> GND
- D46 pad 2: VIN_filtered -> +3.3VA
- D47 pad 1: Net-(D47-K) -> GND
- D47 pad 2: VIN -> +3.3VA
- D5 pad 1: Net-(D5-K) -> /CANH_2
- D5 pad 2: Net-(D5-A) -> /CANL_2
- D6 pad 1: +15V -> Net-(D6-K)
- D6 pad 2: +15V -> Net-(D6-A)
- D7 pad 1: unconnected-(D7-Ctrl-Pad1) -> Net-(D7-K)
- D7 pad 2: GND_IN -> Net-(D7-A)
- D8 pad 1: Net-(D8-K) -> GND
- D8 pad 2: VIN_filtered -> +3.3VA
- D9 pad 1: Net-(D9-K) -> GND
- D9 pad 2: +5V -> +3.3VA
- J1 pad 4: Net-(D1-A) -> Net-(D3-A)
- L1 pad 1: Net-(D2-CANH) -> Net-(D1-CANH)
- L1 pad 3: Net-(D2-CANL) -> Net-(D1-CANL)
- L10 pad 1: Net-(D23-A) -> Net-(D29-A)
- L10 pad 3: Net-(D23-B) -> Net-(D29-B)
- L11 pad 1: Net-(D24-A) -> Net-(D30-A)
- L11 pad 3: Net-(D24-B) -> Net-(D30-B)
- L12 pad 1: +24V -> Net-(D31-A)
- L12 pad 2: Net-(D29-Vin) -> Net-(L12-Pad2)
- L13 pad 2: Net-(D34-Vin) -> Net-(D33-Vin)
- L14 pad 1: Net-(D26-CANH) -> +24V
- L14 pad 2: /CANH_2 -> Net-(D40-Vin)
- L2 pad 1: Net-(D47-K) -> Net-(D4-CANH)
- L2 pad 2: Net-(D12-A2) -> /CANH_2
- L3 pad 1: /SW1 -> Net-(D12-K)
- L3 pad 2: /SW2 -> Net-(D14-A2)
- L4 pad 1: Net-(D17-A) -> /SW1
- L4 pad 2: Net-(L4-Pad2) -> /SW2
- L5 pad 1: Net-(D18-A) -> Net-(D24-A)
- L5 pad 3: Net-(D18-B) -> Net-(D24-B)
- L6 pad 1: Net-(D19-A) -> Net-(D25-A)
- L6 pad 3: Net-(D19-B) -> Net-(D25-B)
- L7 pad 1: Net-(D20-A) -> Net-(D26-A)
- L7 pad 3: Net-(D20-B) -> Net-(D26-B)
- L8 pad 1: Net-(D21-A) -> Net-(D27-A)
- L8 pad 3: Net-(D21-B) -> Net-(D27-B)
- L9 pad 1: Net-(D22-A) -> Net-(D28-A)
- L9 pad 3: Net-(D22-B) -> Net-(D28-B)
- Q1 pad 2: Net-(D12-A2) -> Net-(D14-A2)
- R1 pad 1: GND -> Net-(C15-Pad1)
- R1 pad 2: BOOT0 -> Net-(D1-CANH)
- R10 pad 1: Net-(U6-VIN) -> Net-(D7-K)
- R10 pad 2: Net-(D8-K) -> GND
- R11 pad 1: Net-(D9-K) -> /OverVoltage
- R11 pad 2: GND -> Net-(R11-Pad2)
- R12 pad 1: Net-(D7-Trim) -> GND
- R12 pad 2: GND1 -> /SHDN_OverVoltage
- R13 pad 1: Net-(D10-K) -> +3.3VA
- R13 pad 2: GND -> Net-(U4--)
- R14 pad 1: Net-(D11-K) -> Net-(U4--)
- R15 pad 1: Net-(U6-EN/UVLO) -> /BkIN_1
- R15 pad 2: VIN_filtered -> Net-(R15-Pad2)
- R16 pad 1: Net-(U6-EN/UVLO) -> GND
- R16 pad 2: GND_IN -> /SHDN_OverCurrent_1
- R17 pad 1: GND_IN -> +3.3VA
- R17 pad 2: Net-(C33-Pad2) -> Net-(U5--)
- R18 pad 1: Net-(R18-Pad1) -> /DAC1
- R18 pad 2: +24V -> Net-(U5--)
- R19 pad 1: GND_IN -> Net-(U5--)
- R19 pad 2: Net-(U6-MODE) -> GND
- R2 pad 1: +3.3V -> Net-(D1-CANL)
- R2 pad 2: NRST -> Net-(C15-Pad1)
- R20 pad 1: Net-(U6-FB) -> /BkIN_8
- R20 pad 2: Net-(R18-Pad1) -> Net-(R20-Pad2)
- R21 pad 1: Net-(U6-RT/SYNC) -> Net-(D14-A2)
- R21 pad 2: GND_IN -> VIN_filtered
- R22 pad 1: Net-(U6-PGOOD) -> GND
- R22 pad 2: VCC -> /SHDN_OverCurrent_2
- R23 pad 1: Net-(U6-FB) -> VIN_filtered
- R23 pad 2: GND_IN -> Net-(U7-VISNS)
- R24 pad 1: Net-(Q3-S) -> Net-(U7-VIN)
- R24 pad 2: Net-(U6-CS) -> Net-(D11-K)
- R25 pad 1: Net-(U6-ISNS(+)) -> +3.3VA
- R25 pad 2: VIN_filtered -> Net-(U6--)
- R26 pad 1: GND_IN -> Net-(U7-EN/UVLO)
- R26 pad 2: Net-(Q3-S) -> VIN_filtered
- R27 pad 1: GND_IN -> Net-(U7-EN/UVLO)
- R27 pad 2: Net-(U6-CSG) -> GND_IN
- R28 pad 1: /Connector_channel_1/ERROR -> /DAC2
- R28 pad 2: /ERROR_Channel_1 -> Net-(U6--)
- R29 pad 1: Net-(D15-K) -> Net-(U6--)
- R29 pad 2: GND_IN -> GND
- R3 pad 1: Net-(R3-Pad1) -> GND
- R3 pad 2: Net-(J1-Pin_3) -> BOOT0
- R30 pad 1: Net-(D16-K) -> GND_IN
- R30 pad 2: GND_IN -> Net-(C44-Pad2)
- R31 pad 1: Net-(D17-A) -> Net-(R31-Pad1)
- R31 pad 2: Net-(L4-Pad2) -> +24V
- R32 pad 1: Net-(L4-Pad4) -> GND_IN
- R32 pad 2: Net-(D17-B) -> Net-(U7-MODE)
- R33 pad 1: Net-(D18-A) -> Net-(U7-FB)
- R33 pad 2: Net-(L5-Pad2) -> Net-(R31-Pad1)
- R34 pad 1: Net-(L5-Pad4) -> Net-(U7-RT/SYNC)
- R34 pad 2: Net-(D18-B) -> GND_IN
- R35 pad 1: Net-(D19-A) -> Net-(U7-PGOOD)
- R35 pad 2: Net-(L6-Pad2) -> VCC
- R36 pad 1: Net-(L6-Pad4) -> Net-(U7-FB)
- R36 pad 2: Net-(D19-B) -> GND_IN
- R37 pad 1: Net-(D20-A) -> Net-(Q3-S)
- R37 pad 2: Net-(L7-Pad2) -> Net-(U7-CS)
- R38 pad 1: Net-(L7-Pad4) -> Net-(U7-ISNS(+))
- R38 pad 2: Net-(D20-B) -> VIN_filtered
- R39 pad 1: Net-(D21-A) -> GND_IN
- R39 pad 2: Net-(L8-Pad2) -> Net-(Q3-S)
- R4 pad 1: Net-(R4-Pad1) -> +3.3V
- R4 pad 2: Net-(J1-Pin_2) -> NRST
- R40 pad 1: Net-(L8-Pad4) -> GND_IN
- R40 pad 2: Net-(D21-B) -> Net-(U7-CSG)
- R41 pad 1: Net-(D22-A) -> Net-(D19-K)
- R41 pad 2: Net-(L9-Pad2) -> GND
- R42 pad 1: Net-(L9-Pad4) -> Net-(D18-Trim)
- R42 pad 2: Net-(D22-B) -> GND1
- R43 pad 1: Net-(D23-A) -> Net-(D20-K)
- R43 pad 2: Net-(L10-Pad2) -> GND
- R44 pad 1: Net-(L10-Pad4) -> Net-(D21-K)
- R44 pad 2: Net-(D23-B) -> GND
- R45 pad 1: Net-(D24-A) -> Net-(D22-K)
- R45 pad 2: Net-(L11-Pad2) -> GND_IN
- R46 pad 1: Net-(L11-Pad4) -> Net-(D23-K)
- R46 pad 2: Net-(D24-B) -> GND_IN
- R47 pad 1: /Connector_channel_2/ERROR -> Net-(D24-A)
- R47 pad 2: /ERROR_Channel_2 -> Net-(L5-Pad2)
- R48 pad 1: Net-(J5-Pin_1) (its old number) -> Net-(L5-Pad4)
- R48 pad 2: Net-(R48-Pad2) -> Net-(D24-B)
- R49 pad 1: Net-(R48-Pad2) -> Net-(D25-A)
- R49 pad 2: Net-(R49-Pad2) -> Net-(L6-Pad2)
- R5 pad 1: Net-(C11-Pad1) -> Net-(R5-Pad1)
- R5 pad 2: Net-(D2-CANH) -> Net-(J1-Pin_3)
- R50 pad 1: Net-(R49-Pad2) -> Net-(L6-Pad4)
- R50 pad 2: Net-(D25-A) -> Net-(D25-B)
- R51 pad 1: Net-(R51-Pad1) -> Net-(D26-A)
- R51 pad 2: Net-(J5-Pin_1) (its old number) -> Net-(L7-Pad2)
- R52 pad 1: Net-(U17--) -> Net-(L7-Pad4)
- R52 pad 2: GND -> Net-(D26-B)
- R53 pad 1: Net-(R53-Pad1) -> Net-(D27-A)
- R53 pad 2: Net-(R51-Pad1) -> Net-(L8-Pad2)
- R54 pad 1: Net-(R54-Pad1) -> Net-(L8-Pad4)
- R54 pad 2: Net-(R53-Pad1) -> Net-(D27-B)
- R55 pad 1: Net-(R55-Pad1) -> Net-(D28-A)
- R55 pad 2: Net-(R54-Pad1) -> Net-(L9-Pad2)
- R56 pad 1: GNDPWR -> Net-(L9-Pad4)
- R56 pad 2: Net-(R55-Pad1) -> Net-(D28-B)
- R57 pad 1: Net-(D27-VIN) -> Net-(D29-A)
- R57 pad 2: Net-(R55-Pad1) -> Net-(L10-Pad2)
- R58 pad 1: Net-(D27-OUTP) -> Net-(L10-Pad4)
- R58 pad 2: Net-(U15-+) -> Net-(D29-B)
- R59 pad 1: Net-(D27-OUTN) -> Net-(D30-A)
- R59 pad 2: Net-(U15--) -> Net-(L11-Pad2)
- R6 pad 1: Net-(D2-CANL) -> Net-(R6-Pad1)
- R6 pad 2: Net-(C11-Pad1) -> Net-(J1-Pin_2)
- R60 pad 1: GND -> Net-(L11-Pad4)
- R60 pad 2: Net-(U15-+) -> Net-(D30-B)
- R61 pad 1: Net-(U15--) -> Net-(D31-A)
- R61 pad 2: Net-(C64-Pad2) -> Net-(L12-Pad2)
- R62 pad 1: Net-(C64-Pad2) -> Net-(L12-Pad4)
- R62 pad 2: /HVDC_MCU -> Net-(D31-B)
- R63 pad 1: Net-(D30-K) -> /Connector_channel_1/ERROR
- R63 pad 2: GNDPWR -> /ERROR_Channel_1
- R64 pad 1: +3.3V -> /Connector_channel_2/ERROR
- R64 pad 2: Net-(U17--) -> /ERROR_Channel_2
- R65 pad 1: Net-(J6-Pin_2) -> Net-(D32-K)
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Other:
- board outline added: 122.5 x 123.5 mm

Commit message: VER1.0: раскидал компоненты на плате
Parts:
- removed L10, L11, L12, L5, L6, L7, L8, L9: ~, Inductor_SMD:L_CommonModeChoke_Coilcraft_0805USB
- removed R47, R48, R49, R50, R51, R52, R53, R54, R55, R56, R57, R58, R59, R60, R61, R62: 0, Resistor_SMD:R_0805_2012Metric_Pad1.20x1.40mm_HandSolder
- removed U10, U11, U12, U13, U14, U15, U16, U17: ~, Package_TO_SOT_SMD:SOT-23-6
- added C78: 100u, Capacitor_Tantalum_SMD:CP_EIA-3528-21_Kemet-B_HandSolder, B.Cu at (101.2, 106.5)
- added C93: 100u, Capacitor_Tantalum_SMD:CP_EIA-3528-21_Kemet-B_HandSolder, B.Cu at (81.2, 106.5)
- added H1: MountingHole, MountingHole:MountingHole_4.3mm_M4, F.Cu at (40.5, 46.5)
- added H2: MountingHole, MountingHole:MountingHole_4.3mm_M4, F.Cu at (40.5, 136.5)
- added H3: MountingHole, MountingHole:MountingHole_4.3mm_M4, F.Cu at (210.5, 46.5)
- added H4: MountingHole, MountingHole:MountingHole_4.3mm_M4, F.Cu at (210.5, 136.5)
- added J10: ~, Connector_Molex:Molex_Mini-Fit_Jr_5569-04A2_2x02_P4.20mm_Horizontal, F.Cu at (169.6, 126.5)
- added J11: ~, Connector_Molex:Molex_Mini-Fit_Jr_5569-04A2_2x02_P4.20mm_Horizontal, F.Cu at (158.6, 126.5)
- added J12: ~, Connector_Molex:Molex_Mini-Fit_Jr_5569-04A2_2x02_P4.20mm_Horizontal, F.Cu at (147.6, 126.5)
- added J13: ~, Connector_Molex:Molex_Mini-Fit_Jr_5569-04A2_2x02_P4.20mm_Horizontal, F.Cu at (136.5, 126.5)
- added J5: ~, Connector_Molex:Molex_Mini-Fit_Jr_5569-02A2_2x01_P4.20mm_Horizontal, F.Cu at (125.0, 126.5)
- added J6: ~, Connector_Molex:Molex_Mini-Fit_Jr_5569-02A2_2x01_P4.20mm_Horizontal, F.Cu at (118.0, 126.5)
- added J7: ~, Connector_Molex:Molex_Mini-Fit_Jr_5569-02A2_2x01_P4.20mm_Horizontal, F.Cu at (111.5, 126.5)
- C1, C100, C101, C102, C103, C104, C105, C106, C11, C12, C13, C14, C15, C18, C19, C2, C20, C21, C22, C25, C26, C29, C3, C30, C33, C34, C35, C36, C37, C39, C4, C40, C41, C43, C45, C48, C5, C51, C57, C58, C59, C6, C60, C61, C62, C63, C64, C65, C66, C67, C68, C69, C7, C70, C71, C72, C73, C74, C75, C76, C77, C79, C8, C80, C81, C82, C85, C86, C87, C88, C89, C90, C91, C92, C94, C95, C96, C97, D10, D34, D41, D46, D47, D8, D9, L13, L14, R10, R11, R12, R13, R14, R15, R17, R18, R19, R20, R25, R28, R29, R35, R41, R42, R43, R44, R45, R46, R65, R66, R67, R68, R69, R70, R72, R73, R76, R80, R81, R82, R83, R85, R89, R9, R93, R94, R95, R96, R97, R98, U4, U5, U6: moved to B.Cu
- C38: value 100u -> 68u
- C52, C53: footprint Capacitor_SMD:C_1210_3225Metric_Pad1.33x2.70mm_HandSolder -> Capacitor_SMD:C_1206_3216Metric_Pad1.33x1.80mm_HandSolder
- J2: footprint Connector_Molex:Molex_Mini-Fit_Jr_5566-04A_2x02_P4.20mm_Vertical -> Connector_Molex:Molex_Mini-Fit_Jr_5569-04A2_2x02_P4.20mm_Horizontal
- moved D12 138.1 mm to (42.0, 122.5), turned to -90 degrees
- moved U20 128.8 mm to (73.2, 108.5), turned to 180 degrees
- moved J3 128.0 mm to (72.5, 47.0), turned to 180 degrees
- moved C58 127.8 mm to (71.5, 56.5)
- moved C57 127.7 mm to (71.5, 54.0)
- moved C62 126.2 mm to (59.5, 56.5)
- moved C61 126.0 mm to (59.5, 54.0)
- moved J2 124.8 mm to (52.5, 126.5), turned to 180 degrees
- moved C60 123.1 mm to (77.5, 56.5)
- moved C59 123.0 mm to (77.5, 54.0)
- moved C64 122.9 mm to (65.5, 56.5)
- moved C63 122.7 mm to (65.5, 54.0)
- moved R63 121.3 mm to (82.0, 51.0)
- moved D24 121.1 mm to (71.5, 56.5), turned to 90 degrees
- moved D22 120.8 mm to (42.0, 128.5)
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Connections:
- C101 pad 2: +3.3VP -> +3V3
- C102 pad 1: +3.3VP -> +3V3
- C95 pad 2: +3.3VP -> +3V3
- D24 pad 6: Net-(D24-A) -> /Connector_channel_1/PWM_L1_P
- D24 pad 7: Net-(D24-B) -> /Connector_channel_1/PWM_L1_N
- D25 pad 6: Net-(D25-A) -> /Connector_channel_1/PWM_H1_P
- D25 pad 7: Net-(D25-B) -> /Connector_channel_1/PWM_H1_N
- D26 pad 6: Net-(D26-A) -> /Connector_channel_1/PWM_L2_P
- D26 pad 7: Net-(D26-B) -> /Connector_channel_1/PWM_L2_N
- D27 pad 6: Net-(D27-A) -> /Connector_channel_1/PWM_H2_P
- D27 pad 7: Net-(D27-B) -> /Connector_channel_1/PWM_H2_N
- D28 pad 6: Net-(D28-A) -> /Connector_channel_2/PWM_L1_P
- D28 pad 7: Net-(D28-B) -> /Connector_channel_2/PWM_L1_N
- D29 pad 6: Net-(D29-A) -> /Connector_channel_2/PWM_H1_P
- D29 pad 7: Net-(D29-B) -> /Connector_channel_2/PWM_H1_N
- D30 pad 6: Net-(D30-A) -> /Connector_channel_2/PWM_L2_P
- D30 pad 7: Net-(D30-B) -> /Connector_channel_2/PWM_L2_N
- D31 pad 6: Net-(D31-A) -> /Connector_channel_2/PWM_H2_P
- D31 pad 7: Net-(D31-B) -> /Connector_channel_2/PWM_H2_N
- D39 pad 2: +3.3VP -> +3V3
- D41 pad 2: +3.3VP -> +3V3
- D43 pad 1: +3.3VP -> +3V3
- J2 pad 1: VIN -> GND_IN
- J2 pad 4: GND_IN -> VIN
- U20 pad 2: +3.3VP -> +3V3
- U3 pad 61: unconnected-(U3-PB8-Pad61) -> /OverVoltage
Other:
- board size 122.5 x 123.5 mm -> 179 x 99 mm
- board text added: "PSFB MCU v1.0"
